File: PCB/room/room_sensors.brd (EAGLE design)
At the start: 90.2 x 89.8 mm, 37 parts, among them U1 BH1750FVI-TR, U2 BME280, U3 CCS811B-JOPD500, U4 SN65HVD11DR, U5 SN65HVD11DR, U6 SN65HVD11DR, U7 SN65HVD11DR, U8 MAX14830ETMT

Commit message: first version of schematic ready
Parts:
- removed U$12: NCP551SN18T1G, NCP551SN_snapEDA:SOP95P275X110-5N
- removed U$14: NCP551SN25T1G, NCP551SN_snapEDA:SOP95P275X110-5N
- added C13, C15, C16, C17, C27, C28, C29: 100nF 50V, rcl:C0805
- added C14: 1uF 16V, rcl:C0805
- added C18, C19, C20, C21, C22, C25, C30, C31: 4u7 16V, rcl:C0805
- added C23, C24: 1u 16V, rcl:C0805
- added C26: 220p, rcl:C0805
- added D1, D2, D3, D4: CDSOT23-0502B, CDSOT23-SM712_snapEDA:SOT-23-3
- added R10, R11, R12, R13, R30, R8, R9: 4k7, rcl:R1206
- added R14: 0R, rcl:R1206
- added R15: 47k, rcl:R1206
- added R16: 680R, rcl:R1206
- added R17, R18, R20, R21, R23, R24, R26, R27, R29: 1k, rcl:R1206
- added R19, R22, R25, R28: 120R, rcl:R1206
- added R5: 33k, rcl:R1206
- added R6, R7: 100k, rcl:R1206
- added U$17, U$18: RT9043GB, NCP551SN_snapEDA:SOP95P275X110-5N
- added Y1: X1G004171001800 12MHz, X1G0041710033_snapEDA:OSCCC250X200X80-4N
- C10, C9: value 100nF 50V -> 2u2 16V
- C2, C3, C4, C5, C6, C7, C8: device rcl:C1206 -> rcl:C0805
- R4: value 100R -> 4k7
- moved C5 246.4 mm to (-174.0, -351.8)
- moved C4 232.4 mm to (-166.4, -332.7)
- moved C10 76.0 mm to (-166.4, -281.9)
- moved C9 66.5 mm to (-166.4, -275.6)
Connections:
- removed net +1V8: C11.1, C8.1, U$12.5, U$3.P$10
- removed net +2V5: C12.1, C7.1, U$14.5, U$3.P$4
- removed net AGND: U8.46
- removed net DGND: U8.10
- removed net EP: U3.11
- removed net V18: U8.48
- removed net VCC: U1.1, U4.8, U5.8, U6.8, U7.8
- removed net VDD: U$7.1, U2.8, U3.6
- removed net VDDIO: U2.6
- removed net VL: U8.9
- removed net VSS: U$7.3
- new net +1V2: C11.1, C7.1, U$17.4, U$17.5, U$3.P$10
- new net +2V8: C12.1, C8.1, R6.2, U$18.5, U$3.P$4
- new net AS312_OUT: U$7.2, U8.16
- new net CLK_12M: U$3.P$13, U$4.11, U8.45, Y1.3
- new net EN: U$17.3, U$18.3
- new net ESP32_EN1: R5.1, R7.2, U$18.4
- new net MAX_IO0: U$8.1B, U8.11
- new net MAX_IO1: U$8.2B, U8.12
- new net MAX_IO10: U8.29
- new net MAX_IO11: U8.30
- new net MAX_IO12: U8.35
- new net MAX_IO13: U8.36
- new net MAX_IO14: U8.37
- new net MAX_IO15: U8.38
- new net MAX_IO2: U$8.3B, U8.13
- new net MAX_IO3: U$8.4B, U8.14
- new net MAX_IO4: U$8.5B, U8.19
- new net MAX_IO5: U$8.6B, U8.20
- new net MAX_IO6: U$8.7B, U8.21
- new net MAX_IO7: U$8.8B, U8.22
- new net MAX_IO8: U8.27
- new net MAX_IO9: U8.28
- new net N$10: U6.4, U8.42
- new net N$11: U6.1, U8.41
- new net N$12: U4.2, U4.3, U8.15
- new net N$13: U5.2, U5.3, U8.23
- new net N$14: C13.1, R12.2, U8.8
- new net N$15: U7.2, U7.3, U8.31
- new net N$16: U6.2, U6.3, U8.39
- new net N$17: C14.1, U8.48
- new net N$18: C22.2, U$4.22
- new net N$19: U$4.17, U$5.+
- new net N$20: U$4.19, U$5.-
- new net N$21: C23.2, R14.2, U$6.-
- new net N$22: C24.2, C26.2, R15.2, R16.1, U$6.+
- new net N$23: C23.1, U$4.23
- new net N$24: C24.1, U$4.24
- new net N$25: C25.1, R16.2, U$4.1
- new net N$26: C25.2, C26.1, R15.1
- new net N$27: C28.1, R17.1, U1.5
- new net N$28: U3.4, U3.5
- new net N$29: R30.1, U3.2
- new net N$3: U4.4, U8.18
- new net N$4: R5.2, R6.1
- new net N$5: U4.1, U8.17
- new net N$6: U5.4, U8.26
- new net N$7: U5.1, U8.25
- new net N$8: U7.4, U8.34
- new net N$9: U7.1, U8.33
- new net RS485_A1: D1.2, R18.2, R19.1, U4.6
- new net RS485_A2: D2.2, R21.2, R22.1, U5.6
- new net RS485_A3: D3.2, R24.2, R25.1, U7.6
- new net RS485_A4: D4.2, R27.2, R28.1, U6.6
- new net RS485_B1: D1.1, R19.2, R20.1, U4.7
- new net RS485_B2: D2.1, R22.2, R23.1, U5.7
- new net RS485_B3: D3.1, R25.2, R26.1, U7.7
- new net RS485_B4: D4.1, R28.2, R29.1, U6.7
- new net SPKGND: C18.2, C19.2, C20.2, C21.2, U$4.18, U$4.3, U$4.6, U$4.EP
- new net SPKVDD: C18.1, C19.1, C20.1, C21.1, U$4.2, U$4.20, U$4.4, U$4.5
- net +3V3: now also C15.1, C16.1, C17.1, C27.1, C29.1, C30.1, C31.1, C5.1, R10.2, R11.2, R12.1, R13.1, R17.2, R18.1, R21.1, R24.1, R27.1, R30.2, R8.2, R9.2, U$17.1, U$18.1, U$7.1, U$8.1A, U$8.2A, U$8.3A, U$8.4A, U$8.5A, U$8.6A, U$8.7A, U$8.8A, U1.1, U2.2, U2.6, U2.8, U3.6, U4.8, U5.8, U6.8, U7.8, U8.1, U8.2, U8.43, U8.47, U8.9, Y1.4; no longer U$12.1, U$12.3, U$14.1, U$14.3
- net ESP32_BOOT: no longer C5.1
- net ESP32_EN: no longer C4.1
- net ESP32_IO0: now also R11.1, U$4.13, U1.6
- net ESP32_IO1: now also U$4.8
- net ESP32_IO18: now also U8.4
- net ESP32_IO19: now also U8.3
- net ESP32_IO2: now also R10.1, U$3.P$5
- net ESP32_IO21: now also R13.2, U8.7; no longer U$3.P$13
- net ESP32_IO23: now also U8.6; no longer U$3.P$9
- net ESP32_IO26: now also R9.1
- net ESP32_IO27: now also U$3.P$9; no longer U$3.P$5
- net ESP32_IO3: now also U$4.10
- net ESP32_IO32: now also U$4.7
- net ESP32_IO33: now also R8.1, U$4.14, U1.4
- net ESP32_IO4: now also U$4.9
- net ESP32_IO5: now also U8.5
- net GND: now also C13.2, C14.2, C15.2, C16.2, C17.2, C22.1, C27.2, C28.2, C29.2, C30.2, C31.2, D1.3, D2.3, D3.3, D4.3, R14.1, R20.2, R23.2, R26.2, R29.2, R7.1, U$17.2, U$18.2, U$4.15, U$7.3, U1.2, U2.5, U3.1, U3.11, U3.7, U4.5, U5.5, U6.5, U7.5, U8.10, U8.46, U8.49, Y1.2; no longer U$12.2, U$14.2
- net N$2: now also C4.1

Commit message: Placement done
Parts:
- removed U$1, U$2: 95278-101A14LF, 95278-101A14LF_snapEDA:95278-101A14LF
- removed U$17, U$18: RT9043GB, NCP551SN_snapEDA:SOP95P275X110-5N
- removed U$3: OV2640-HDF3M-811FRONTLOOKING, parts:FH34SRJ-24S-0.5SH(50)
- removed U$4: WM8974, WM8974_snapEDA:QFN-24_ALT2
- removed U$5: SMS-208MS-R, speaker_snapEDA:SMS-2008MS-R
- removed U$8: DHN-08F-T-V-T/R], parts:DHN-08F-T-V-T/R]
- added C32, C33, C34, C35: 100nF 50V, rcl:C0805
- added CON1, CON2: 95278-101A14LF, 95278-101A14LF_snapEDA:95278-101A14LF
- added CON3: OV2640-HDF3M-811FRONTLOOKING, parts:FH34SRJ-24S-0.5SH(50)
- added S8: DHN-08F-T-V-T/R], parts:DHN-08F-T-V-T/R]
- added SPR1: SMS-208MS-R, speaker_snapEDA:SMS-2008MS-R
- added U14: WM8974, WM8974_snapEDA:QFN-24_ALT2
- added U17, U18: RT9043GB, NCP551SN_snapEDA:SOP95P275X110-5N
- moved C29 710.4 mm to (44.5, 76.2), turned to 180 degrees
- moved C31 689.2 mm to (45.7, 34.3), turned to 90 degrees
- moved R30 681.8 mm to (19.1, 41.9)
- moved C30 678.5 mm to (19.1, 44.5)
- moved C26 669.8 mm to (74.9, 47.0), turned to 180 degrees
- moved R17 667.5 mm to (31.8, 41.9)
- moved R16 666.5 mm to (73.7, 50.8), turned to 90 degrees
- moved C25 662.1 mm to (76.2, 50.8), turned to 270 degrees
- moved C28 660.3 mm to (26.7, 41.9), turned to 180 degrees
- moved C27 656.6 mm to (26.7, 44.5)
- moved R15 654.4 mm to (78.7, 48.3), turned to 270 degrees
- moved C24 644.4 mm to (69.8, 53.3)
- moved R14 643.9 mm to (69.8, 47.0)
- moved C23 635.0 mm to (69.8, 49.5)
- moved C22 630.7 mm to (64.8, 53.3), turned to 180 degrees
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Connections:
- removed net EN: U$17.3, U$18.3
- removed net ESP32_IO10: A1.18
- removed net ESP32_IO11: A1.19
- removed net ESP32_IO6: A1.20
- removed net ESP32_IO7: A1.21
- removed net ESP32_IO8: A1.22
- removed net ESP32_IO9: A1.17
- removed net RS485_A4: D4.2, R27.2, R28.1, U6.6
- removed net RS485_B4: D4.1, R28.2, R29.1, U6.7
- removed net SPKGND: C18.2, C19.2, C20.2, C21.2, U$4.18, U$4.3, U$4.6, U$4.EP
- removed net SPKVDD: C18.1, C19.1, C20.1, C21.1, U$4.2, U$4.20, U$4.4, U$4.5
- new net RS485_A0: CON2.1, D1.2, R18.2, R19.1, U4.6
- new net RS485_B0: CON2.2, D1.1, R19.2, R20.1, U4.7
- net +1V2: now also CON3.P$10, U17.4, U17.5; no longer U$17.4, U$17.5, U$3.P$10
- net +2V8: now also CON3.P$4, U18.5; no longer U$18.5, U$3.P$4
- net +3V3: now also C18.1, C19.1, C20.1, C21.1, C32.1, C33.1, C34.1, C35.1, CON1.2, CON1.4, CON3.P$11, S8.1A, S8.2A, S8.3A, S8.4A, S8.5A, S8.6A, S8.7A, S8.8A, U14.2, U14.20, U14.4, U14.5, U17.1, U17.3, U18.1, U18.3; no longer U$17.1, U$18.1, U$3.P$11, U$8.1A, U$8.2A, U$8.3A, U$8.4A, U$8.5A, U$8.6A, U$8.7A, U$8.8A
- net CLK_12M: now also CON3.P$13, U14.11; no longer U$3.P$13, U$4.11
- net ESP32_EN1: now also U18.4; no longer U$18.4
- net ESP32_IO0: now also CON1.13, U14.13, U2.4, U3.10; no longer U$4.13
- net ESP32_IO1: now also CON2.9, U14.8; no longer U$4.8
- net ESP32_IO12: now also CON2.11, CON3.P$21; no longer U$3.P$21
- net ESP32_IO13: now also CON2.13, CON3.P$22; no longer U$3.P$22
- net ESP32_IO14: now also CON2.12, CON3.P$19; no longer U$3.P$19
- net ESP32_IO15: now also CON2.14, CON3.P$20; no longer U$3.P$20
- net ESP32_IO2: now also CON3.P$5; no longer U$3.P$5
- net ESP32_IO22: now also CON3.P$17; no longer U$3.P$17
- net ESP32_IO25: now also A1.10, CON3.P$7; no longer U$3.P$7
- net ESP32_IO26: now also CON3.P$3; no longer U$3.P$3
- net ESP32_IO27: now also CON3.P$9; no longer U$3.P$9
- net ESP32_IO3: now also CON2.10, U14.10; no longer U$4.10
- net ESP32_IO32: now also U14.7; no longer U$4.7
- net ESP32_IO33: now also CON1.14, U14.14, U2.3, U3.9; no longer U$4.14
- net ESP32_IO34: now also CON3.P$18; no longer U$3.P$18
- net ESP32_IO35: now also CON3.P$16; no longer A1.10, U$3.P$16
- net ESP32_IO36: now also CON3.P$12; no longer U$3.P$12
- net ESP32_IO39: now also CON3.P$14; no longer U$3.P$14
- net ESP32_IO4: now also U14.9; no longer U$4.9
- net GND: now also C18.2, C19.2, C20.2, C21.2, C32.2, C33.2, C34.2, C35.2, CON1.1, CON1.3, CON3.P$15, CON3.P$2, U14.15, U14.18, U14.3, U14.6, U14.EP, U17.2, U18.2; no longer U$17.2, U$18.2, U$3.P$15, U$3.P$2, U$4.15
- net MAX_IO0: now also S8.1B; no longer U$8.1B
- net MAX_IO1: now also S8.2B; no longer U$8.2B
- net MAX_IO10: now also CON1.10
- net MAX_IO11: now also CON1.12
- net MAX_IO12: now also CON1.11
- net MAX_IO13: now also CON1.9
- net MAX_IO14: now also CON1.7
- net MAX_IO15: now also CON1.5
- net MAX_IO2: now also S8.3B; no longer U$8.3B
- net MAX_IO3: now also S8.4B; no longer U$8.4B
- net MAX_IO4: now also S8.5B; no longer U$8.5B
- net MAX_IO5: now also S8.6B; no longer U$8.6B
- net MAX_IO6: now also S8.7B; no longer U$8.7B
- net MAX_IO7: now also S8.8B; no longer U$8.8B
- net MAX_IO8: now also CON1.6
- net MAX_IO9: now also CON1.8
- net N$1: now also CON3.P$8; no longer U$3.P$8
- net N$18: now also U14.22; no longer U$4.22
- net N$19: now also SPR1.+, U14.17; no longer U$4.17, U$5.+
- net N$2: now also CON3.P$6; no longer U$3.P$6
- net N$20: now also SPR1.-, U14.19; no longer U$4.19, U$5.-
- net N$23: now also U14.23; no longer U$4.23
- net N$24: now also U14.24; no longer U$4.24
- net N$25: now also U14.1; no longer U$4.1
- net RS485_A1: now also CON2.3, D2.2, R21.2, R22.1, U5.6; no longer D1.2, R18.2, R19.1, U4.6
- net RS485_A2: now also CON2.5, D3.2, R24.2, R25.1, U7.6; no longer D2.2, R21.2, R22.1, U5.6
- net RS485_A3: now also CON2.7, D4.2, R27.2, R28.1, U6.6; no longer D3.2, R24.2, R25.1, U7.6
- net RS485_B1: now also CON2.4, D2.1, R22.2, R23.1, U5.7; no longer D1.1, R19.2, R20.1, U4.7
- net RS485_B2: now also CON2.6, D3.1, R25.2, R26.1, U7.7; no longer D2.1, R22.2, R23.1, U5.7
- net RS485_B3: now also CON2.8, D4.1, R28.2, R29.1, U6.7; no longer D3.1, R25.2, R26.1, U7.7

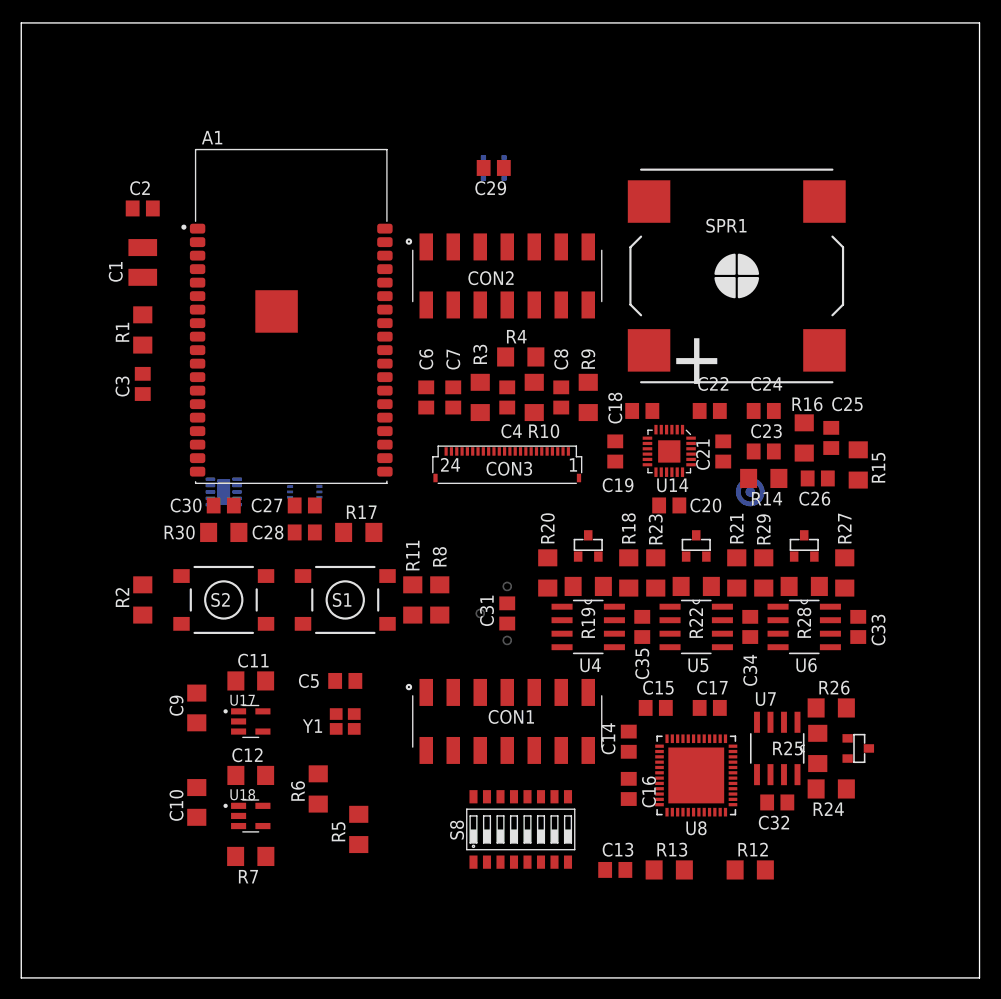
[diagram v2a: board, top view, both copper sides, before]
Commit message: finished routing for room sensor PCB
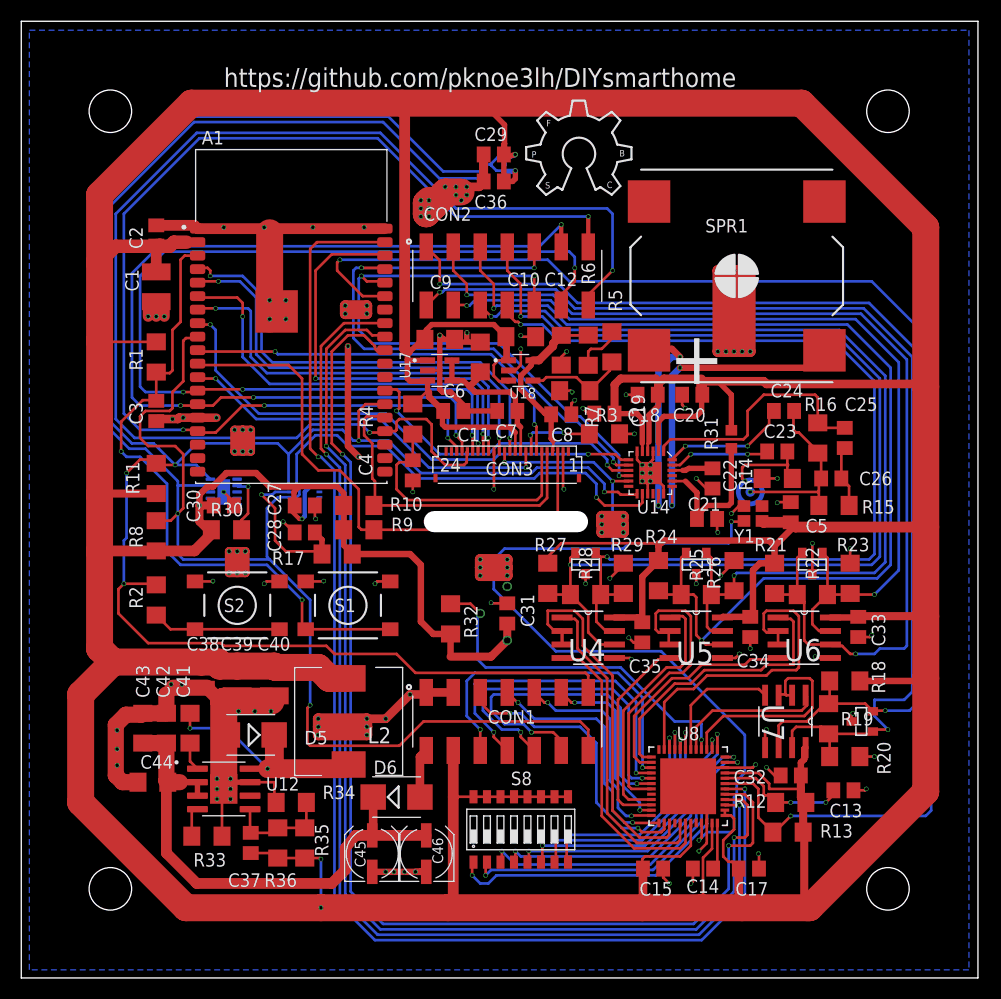
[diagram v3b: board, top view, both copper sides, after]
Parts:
- removed C16: 100nF 50V, rcl:C0805
- added C36: 100nF 50V, rcl:C0805
- added C37: NM, rcl:C0805
- added C38: 1uF 16V, rcl:C0805
- added C39, C40: 47u 10V, rcl:C1210
- added C41, C42: 100n 50V, rcl:C1206
- added C43, C44: 2u2 50V, rcl:C1206
- added C45, C46: 47u 35V, rcl:UD-5X5,8_NICHICON
- added D5, D6: B360B-13-F, diode:SMB
- added L2: 5u6 3A8, parts:SLF10145T-150M2R2-PF
- added LOGO1: OSHW_LOGO_FILLX0350-NT, ohw-logo:OSHW_FILLX350_NOTEXT
- added R31: 0R, rcl:R0603
- added R32: 1k, rcl:R1206
- added R33: 33k, rcl:R1206
- added R34: 12k, rcl:R1206
- added R35: 68k, rcl:R1206
- added R36: 100k, rcl:R1206
- added U12: LMR16020, LMR160X0_snapEDA:SOIC127P600X170-8N
- moved C10 53.4 mm to (47.0, 60.3), turned to 0 degrees
- moved R7 53.4 mm to (52.1, 55.2)
- moved R5 51.3 mm to (55.6, 59.4)
- moved C12 49.5 mm to (50.8, 59.1), turned to 270 degrees
- moved U18 49.0 mm to (47.0, 57.1)
- moved R6 48.5 mm to (53.3, 59.1)
- moved C5 44.8 mm to (72.4, 43.8), turned to 90 degrees
- moved Y1 43.1 mm to (68.8, 43.7), turned to 180 degrees
- moved C9 41.5 mm to (39.4, 60.1), turned to 0 degrees
- moved U17 37.5 mm to (39.4, 57.1)
- moved C11 37.4 mm to (43.2, 58.4), turned to 90 degrees
- moved R20 32.8 mm to (77.5, 20.8), turned to 0 degrees
- moved D1 30.6 mm to (79.1, 24.1), turned to 90 degrees
- moved R27 27.9 mm to (49.5, 37.6)
- moved R8 27.3 mm to (12.7, 41.6)
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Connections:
- new net +24V: C42.1, C43.1, C44.1, C45.+, C46.+, D6.C, U12.2, U12.3
- new net N$30: C21.2, R31.2, U14.20
- new net N$31: CON1.2, D6.A
- new net N$32: R33.1, U12.4
- new net N$33: C37.2, R34.1, R35.2, R36.2, U12.5
- new net N$34: C41.2, D5.C, L2.P$1, U12.8
- new net N$35: C41.1, U12.1
- net +3V3: now also C36.1, C37.1, C38.1, C39.1, C40.1, L2.P$2, R31.1, R32.2, R35.1, R36.1; no longer C16.1, C21.1, CON1.2, U14.20
- net AS312_OUT: now also R32.1
- net GND: now also C21.1, C36.2, C38.2, C39.2, C40.2, C42.2, C43.2, C44.2, C45.-, C46.-, D5.A, R33.2, R34.2, U12.7, U12.9; no longer C16.2, C21.2
- net N$10: now also U4.4; no longer U6.4
- net N$11: now also U4.1; no longer U6.1
- net N$12: now also U7.2, U7.3; no longer U4.2, U4.3
- net N$13: now also U6.2, U6.3; no longer U5.2, U5.3
- net N$15: now also U5.2, U5.3; no longer U7.2, U7.3
- net N$16: now also U4.2, U4.3; no longer U6.2, U6.3
- net N$3: now also U7.4; no longer U4.4
- net N$5: now also U7.1; no longer U4.1
- net N$6: now also U6.4; no longer U5.4
- net N$7: now also U6.1; no longer U5.1
- net N$8: now also U5.4; no longer U7.4
- net N$9: now also U5.1; no longer U7.1
- net RS485_A0: now also U7.6; no longer U4.6
- net RS485_A1: now also U6.6; no longer U5.6
- net RS485_A2: now also U5.6; no longer U7.6
- net RS485_A3: now also U4.6; no longer U6.6
- net RS485_B0: now also U7.7; no longer U4.7
- net RS485_B1: now also U6.7; no longer U5.7
- net RS485_B2: now also U5.7; no longer U7.7
- net RS485_B3: now also U4.7; no longer U6.7
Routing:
- net +3V3: track 0.00 -> 745.9 mm, vias 0 -> 6
- net GND: track 0.00 -> 357.6 mm, vias 0 -> 147
- net ESP32_IO33: track 0.00 -> 215.9 mm, vias 0 -> 3
- net ESP32_IO0: track 0.00 -> 200.4 mm, vias 0 -> 5
- net ESP32_IO21: track 0.00 -> 133.5 mm, vias 0 -> 2
- net ESP32_IO23: track 0.00 -> 123.5 mm, vias 0 -> 2
- net ESP32_IO15: track 0.00 -> 121.9 mm, vias 0 -> 2
- net ESP32_IO19: track 0.00 -> 109.9 mm, vias 0 -> 2
- net ESP32_IO18: track 0.00 -> 109.6 mm, vias 0 -> 2
- net ESP32_IO5: track 0.00 -> 109.4 mm, vias 0 -> 2
- net ESP32_IO13: track 0.00 -> 108.0 mm, vias 0 -> 4
- net RS485_A0: track 0.00 -> 103.7 mm, vias 0 -> 2
- net RS485_A3: track 0.00 -> 103.4 mm, vias 0 -> 2
- net RS485_B0: track 0.00 -> 101.0 mm, vias 0 -> 2
- net RS485_A2: track 0.00 -> 99.7 mm, vias 0 -> 2
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- added copper zone on layer 16, net GND
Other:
- board size 90.2 x 89.8 mm -> 90 x 90 mm
- board text added: "https://github.com/pknoe3lh/DIYsmarthome"
